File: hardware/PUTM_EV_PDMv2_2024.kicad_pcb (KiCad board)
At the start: 4 copper layers, 85 x 58 mm, 171 parts, among them IC1 BTS722204ESAXUMA1, IC2 BTS722204ESAXUMA1, IC3 BTS722204ESAXUMA1, IC4 BTS722204ESAXUMA1, J1 74650073R, J2 IPBS-110-01-XX-D-GP, J3 FTSH-107-01-L-D-K, Q1 30V/5A, T1 TP_VCC, T2 TP_GND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

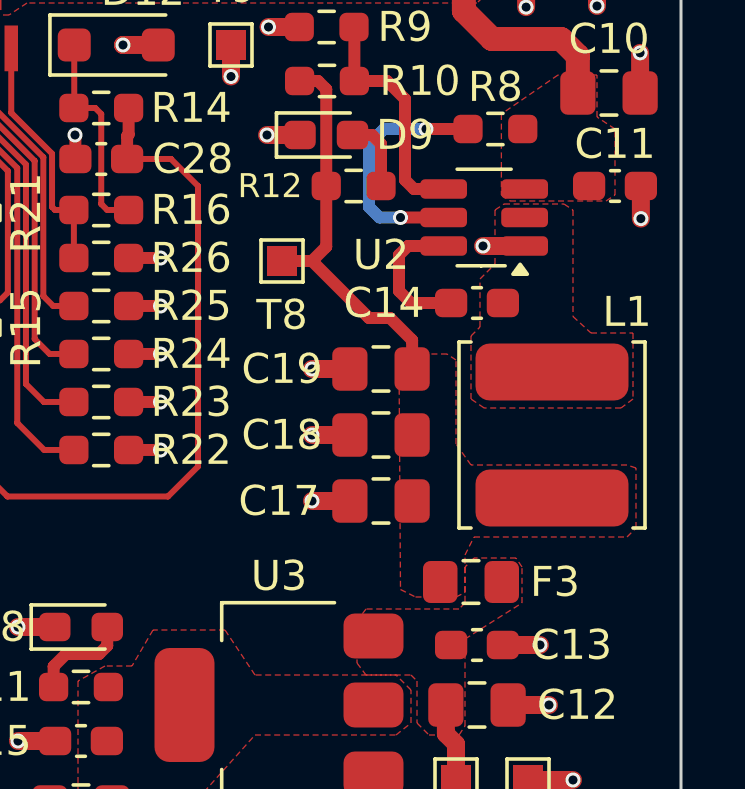
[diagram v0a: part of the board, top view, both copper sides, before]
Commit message: pcb layout-power section 5V update
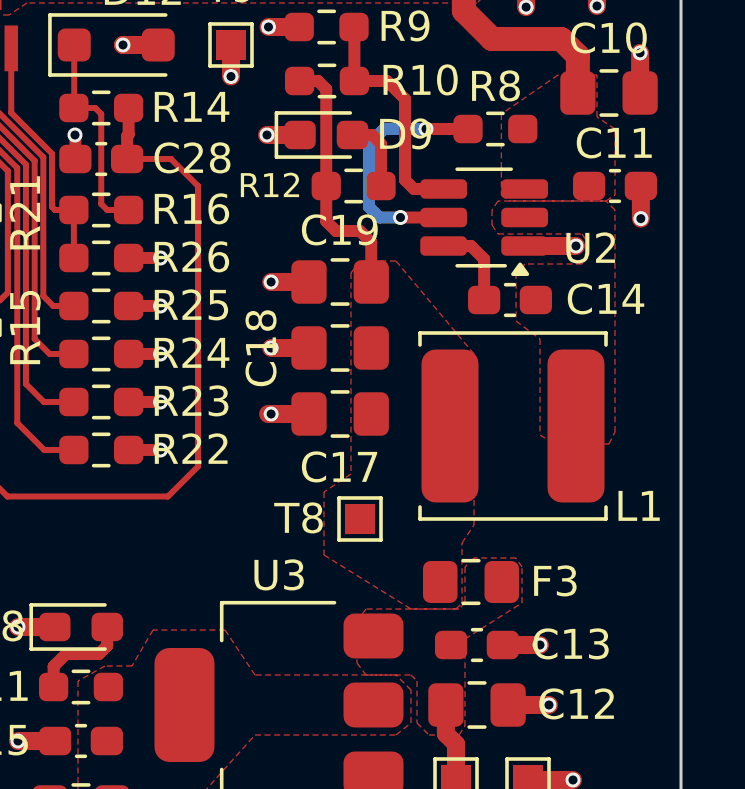
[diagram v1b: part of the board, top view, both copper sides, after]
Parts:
- moved T8 8.98 mm to (194.3, 104.8)
- moved C17 3.20 mm to (193.6, 101.3)
- moved C18 3.20 mm to (193.6, 99.1)
- moved C19 3.20 mm to (193.6, 96.9)
- moved L1 1.33 mm to (199.4, 101.7), turned to 180 degrees
- moved C14 1.10 mm to (199.3, 97.5)
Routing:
- net /Power/+5V_OUT: track 13.3 -> 8.52 mm
- net /Power/BOOT_+5V: track 4.71 -> 2.89 mm

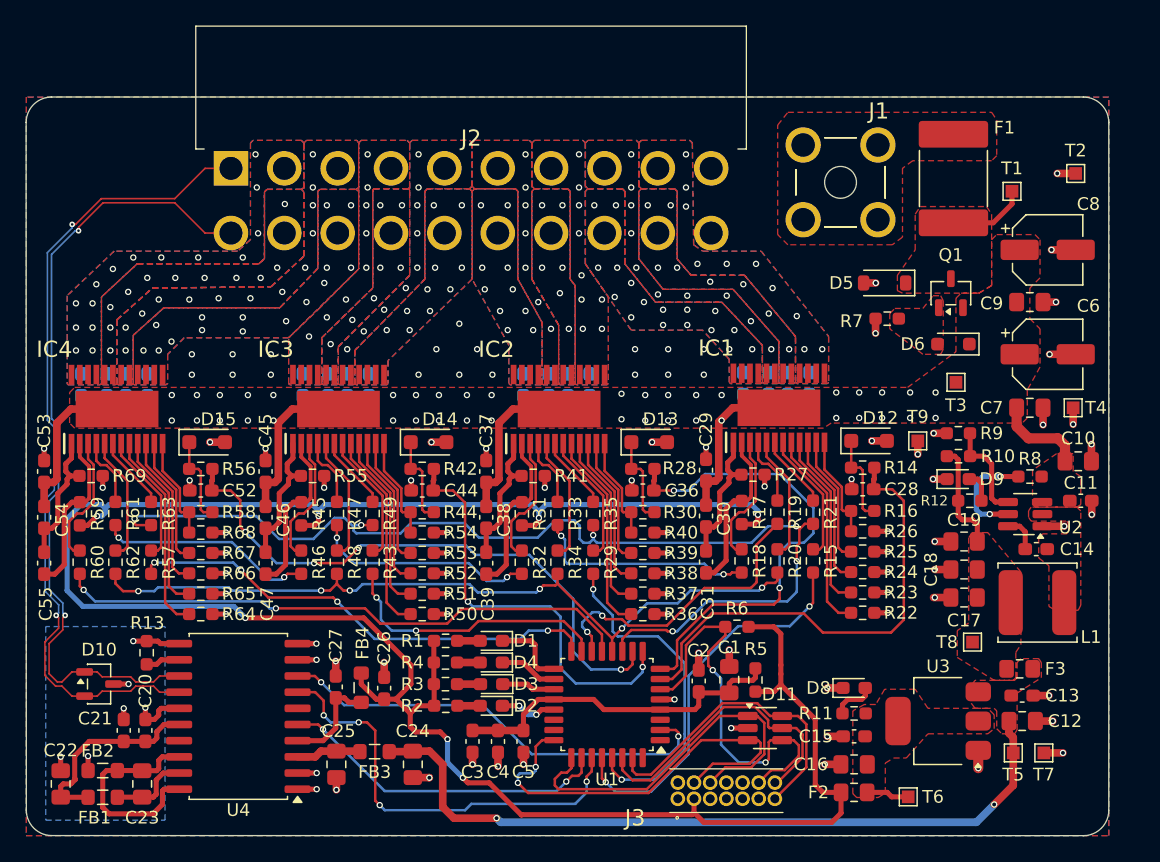
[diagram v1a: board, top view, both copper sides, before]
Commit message: pcb layout - controlers power->battery, added mounting holes
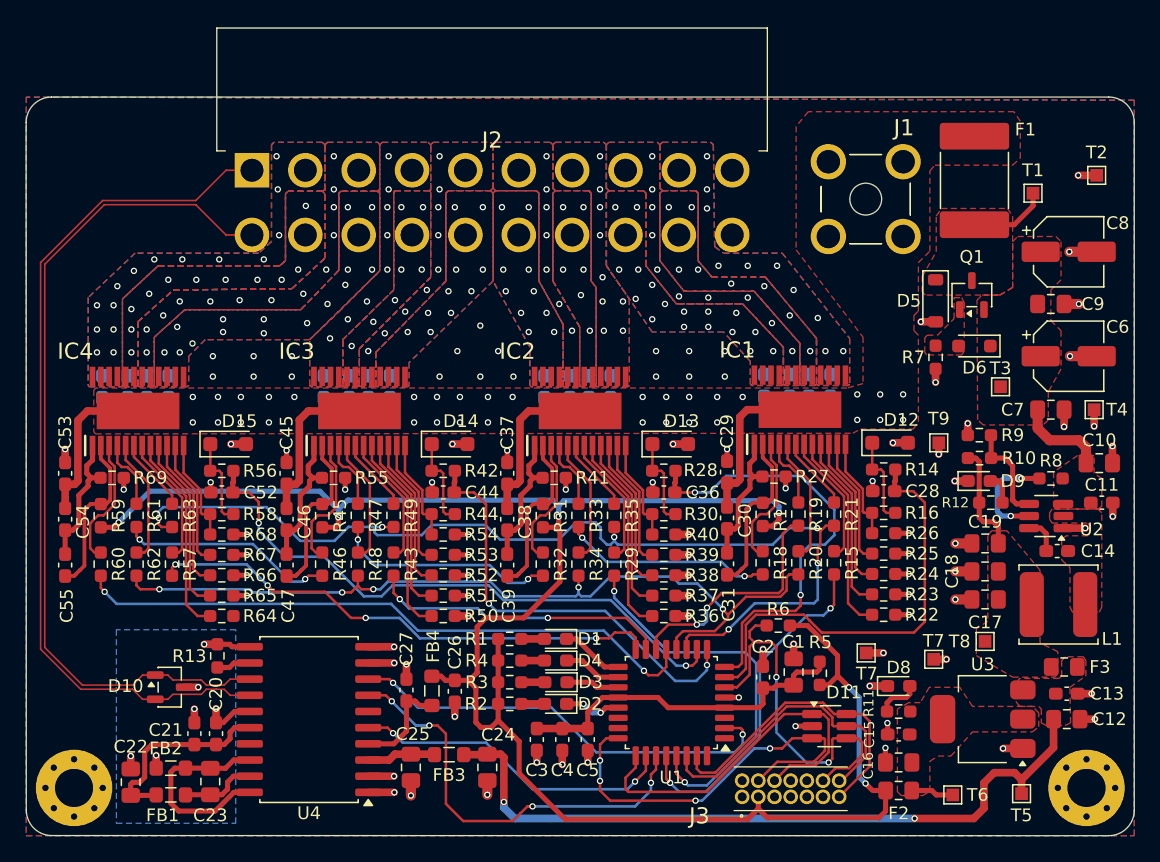
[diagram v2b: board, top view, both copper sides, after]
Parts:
- removed the T7 at (199.9, 113.5)
- added REF**: MountingHole_3mm_Pad_Via, MountingHole:MountingHole_3mm_Pad_Via, F.Cu at (123.8, 116.2)
- added REF**: MountingHole_3mm_Pad_Via, MountingHole:MountingHole_3mm_Pad_Via, F.Cu at (203.2, 116.2)
- added T7: TP_GND, TestPoint:TestPoint_Pad_1.0x1.0mm, F.Cu at (191.2, 106.2)
- added T7: TP_GND, TestPoint:TestPoint_Pad_1.0x1.0mm, F.Cu at (185.9, 105.7)
- moved C24 5.85 mm to (156.2, 114.6)
- moved C25 5.85 mm to (150.2, 114.6)
- moved FB3 5.85 mm to (153.2, 113.6)
- moved C20 5.55 mm to (134.9, 112.0)
- moved C21 5.55 mm to (133.2, 112.0)
- moved C26 5.55 mm to (153.6, 108.7), turned to -90 degrees
- moved R13 5.55 mm to (135.0, 105.9)
- moved U4 5.55 mm to (142.2, 110.9)
- moved D10 5.55 mm to (131.3, 108.3)
- moved C27 5.55 mm to (149.8, 108.6)
- moved FB4 5.55 mm to (151.8, 108.6)
- moved C22 5.50 mm to (128.2, 115.8)
- moved C23 5.35 mm to (134.4, 115.7)
- moved FB2 5.35 mm to (131.3, 114.7)
- moved FB1 5.35 mm to (131.3, 116.8)
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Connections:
- C29 pad 1: +24V -> +BATT
- C30 pad 1: +24V -> +BATT
- C37 pad 1: +24V -> +BATT
- C38 pad 1: +24V -> +BATT
- C45 pad 1: +24V -> +BATT
- C46 pad 1: +24V -> +BATT
- C53 pad 1: +24V -> +BATT
- C54 pad 1: +24V -> +BATT
- IC1 pad 25: +24V -> +BATT
- IC2 pad 25: +24V -> +BATT
- IC3 pad 25: +24V -> +BATT
- IC4 pad 25: +24V -> +BATT
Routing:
- net +BATT: track 0.00 -> 51.2 mm, vias 0 -> 33
- net +24V: track 57.4 -> 7.12 mm, vias 40 -> 0
- net +3V3: track 179.1 -> 153.2 mm, vias 7 -> 6
- net /MCU/SPI.SCK: track 61.3 -> 66.1 mm, vias 6 -> 5
- net /CAN/CAN.P: track 63.8 -> 68.5 mm, vias 2 -> 0
- net /CAN/CAN.N: track 62.7 -> 67.4 mm, vias 2 -> 0
- net /MCU/SPI.MOSI: track 23.7 -> 19.0 mm
- net /MCU/SPI.MISO: track 45.8 -> 49.8 mm
- net /MCU/LHI1: track 26.6 -> 30.4 mm
- net /MCU/LHI0: track 30.8 -> 27.3 mm
- net /MCU/SPI.NSS: track 84.9 -> 81.5 mm
- net /MCU/LHI3: track 37.8 -> 40.9 mm
- net /MCU/FUSE_IS0: track 37.3 -> 34.5 mm
- net /MCU/FUSE_IS1: track 37.6 -> 35.0 mm
- net /MCU/LHI2: track 21.9 -> 23.5 mm
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- added copper zone on In1.Cu, net +BATT
- added copper zone on In2.Cu, net +BATT
- removed copper zone on In1.Cu, net +24V
- removed copper zone on In2.Cu, net +24V
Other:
- board size 85 x 58 mm -> 87 x 58 mm
